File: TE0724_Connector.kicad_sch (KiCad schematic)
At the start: 2 parts, among them J1 SS5-80-3.50-L-D-K-TR, J3 Conn_02x05_Odd_Even

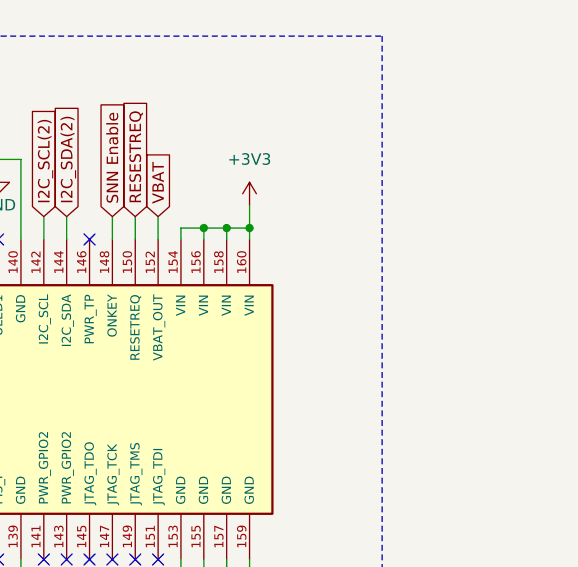
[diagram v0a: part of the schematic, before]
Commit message: Added some decoup caps and reviewed PCB layout
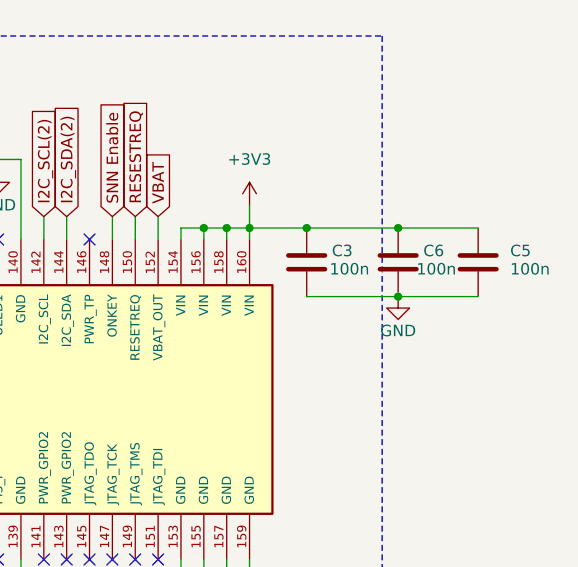
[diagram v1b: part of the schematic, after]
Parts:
- added C3, C5, C6: 100n, Capacitor_SMD:C_0603_1608Metric, symbol Device:C
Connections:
- net +3V3: now also C3.1, C5.1, C6.1
- net GND: now also C3.2, C5.2, C6.2

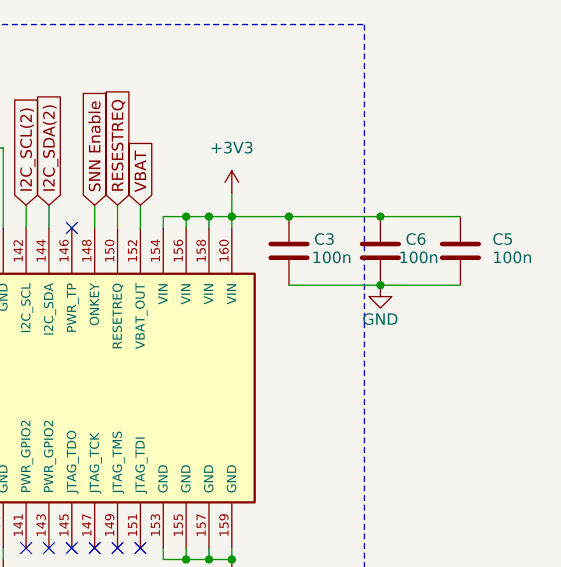
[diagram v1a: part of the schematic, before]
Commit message: removed some decoup caps because I added to many haha
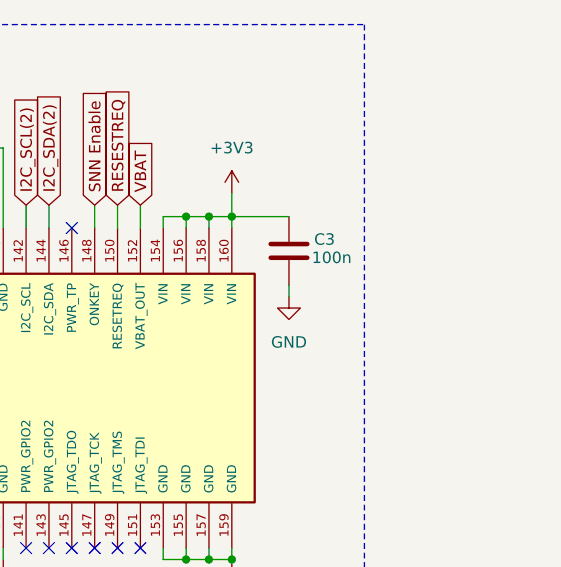
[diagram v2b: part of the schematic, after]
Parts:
- removed C5, C6: 100n, Capacitor_SMD:C_0603_1608Metric, symbol Device:C

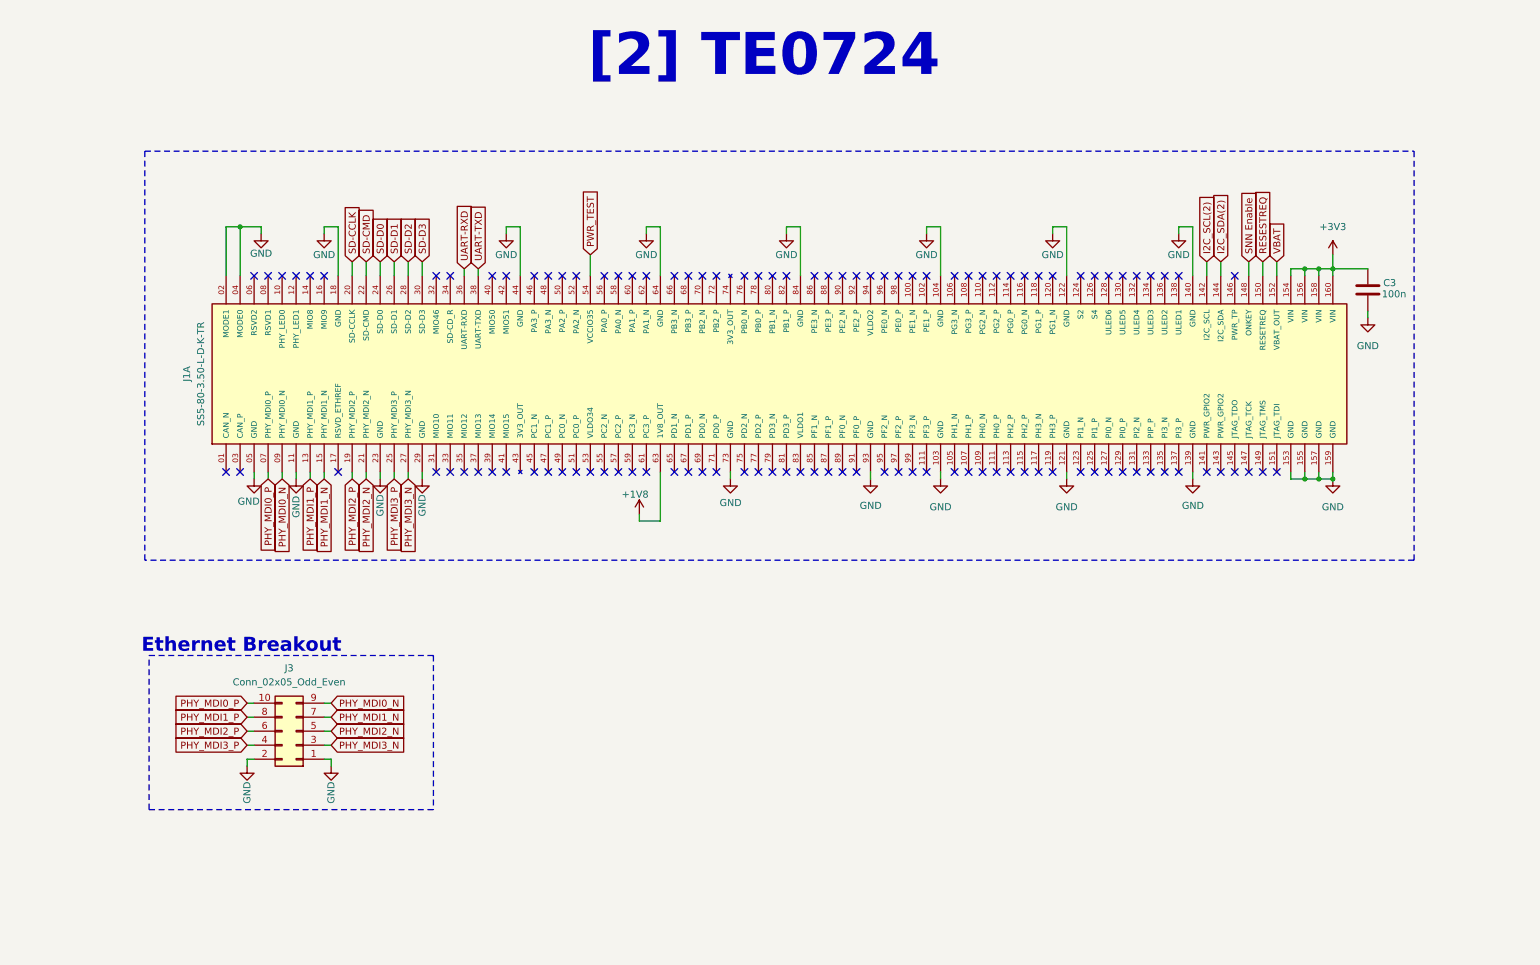
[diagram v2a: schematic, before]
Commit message: Added Level Shifter for SD card
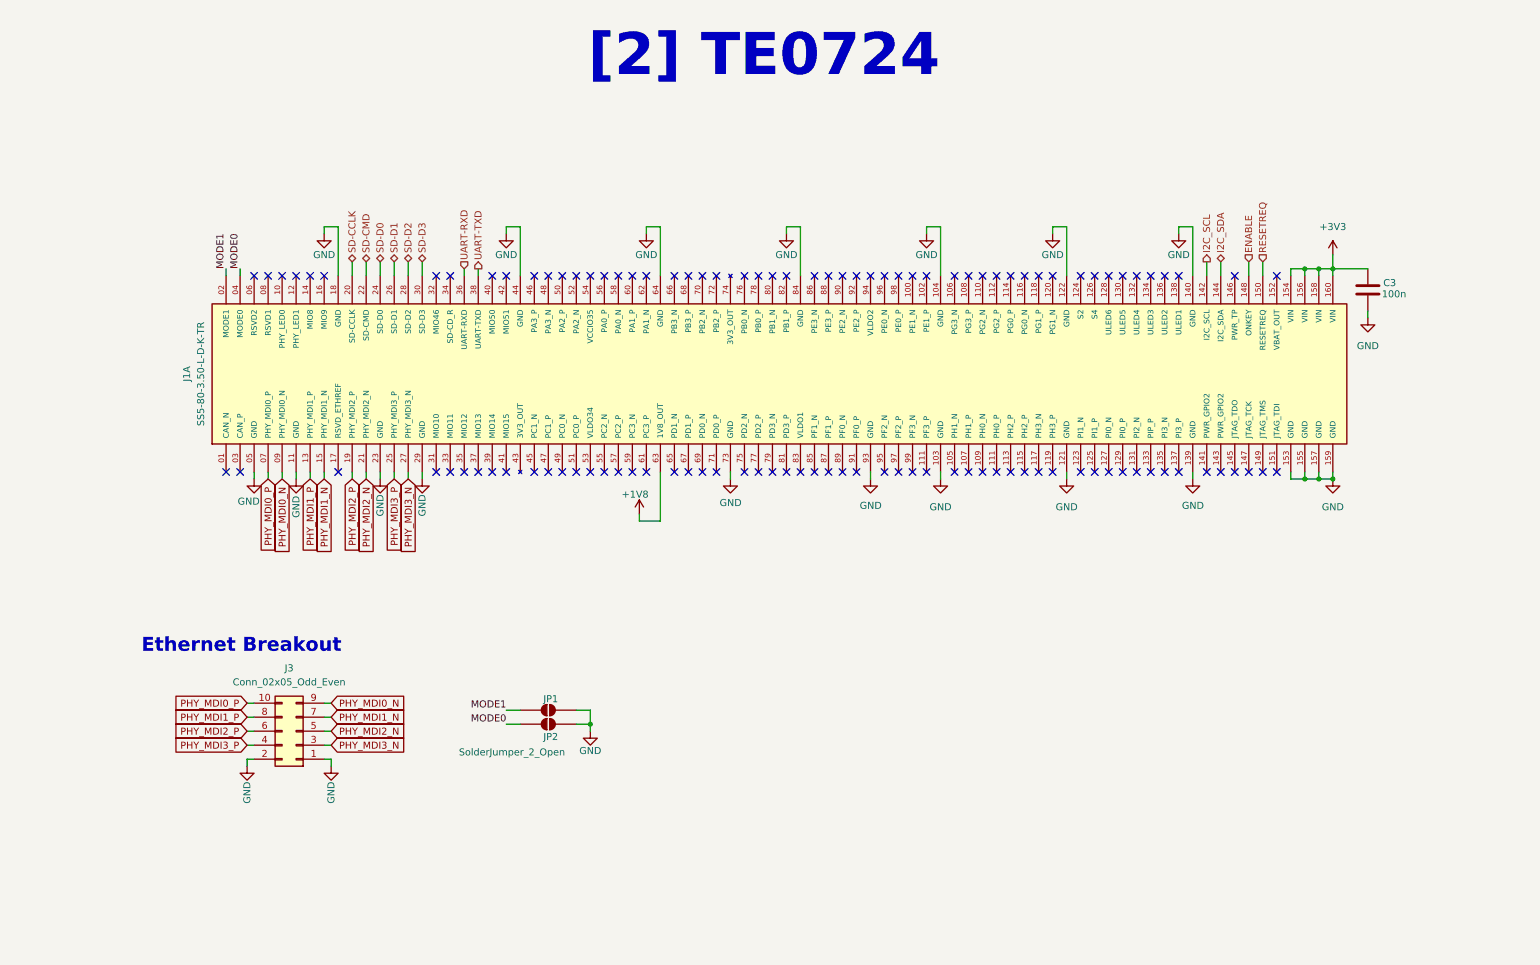
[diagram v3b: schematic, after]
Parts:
- added JP1, JP2: SolderJumper_2_Open, Jumper:SolderJumper-2_P1.3mm_Open_RoundedPad1.0x1.5mm, symbol Jumper:SolderJumper_2_Open
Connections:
- net GND: now also JP1.2 (B), JP2.2 (B); no longer J1.02 (MODE1), J1.04 (MODE0)
- net I2C_SCL(2) renamed I2C_SCL
- net I2C_SDA(2) renamed I2C_SDA
- net PWR_TEST: no longer names the net of J1.54 (VCCIO35)
- net RESESTREQ renamed RESETREQ
- net SNN Enable renamed ENABLE
- net VBAT: no longer names the net of J1.152 (VBAT_OUT)
- new net MODE0: J1.04 (MODE0), JP2.1 (A)
- new net MODE1: J1.02 (MODE1), JP1.1 (A)
- no-connect marks 109 -> 111

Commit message: Added pcb files for ethernet breakout board
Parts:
- J1: MPN (none) -> C5292077
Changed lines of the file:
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@@
+			)
+		)
+		(property "External Part Number" ""
+			(at 97.79 85.09 0)
+			(hide yes)
+			(show_name no)
+			(do_not_autoplace no)
+			(effects
+				(font
+					(size 1.27 1.27)
+				)
+			)
+		)
+		(property "MPN" "C5292077"
+			(at 97.79 85.09 0)
+			(hide yes)
+			(show_name no)
+			(do_not_autoplace no)
+			(effects
+				(font
+					(size 1.27 1.27)
+				)
 			)
 		)
@@
 			)
 		)
+		(property "External Part Number" ""
+			(at 107.95 148.59 0)
+			(hide yes)
+			(show_name no)
+			(do_not_autoplace no)
+			(effects
+				(font
+					(size 1.27 1.27)
+				)
+			)
+		)
+		(property "MPN" ""
+			(at 107.95 148.59 0)
+			(hide yes)
+			(show_name no)
+			(do_not_autoplace no)
+			(effects
+				(font
+					(size 1.27 1.27)
+				)
+			)
+		)
 		(pin "1"
 		)
@@
 			)
 		)
+		(property "External Part Number" ""
+			(at 107.95 146.05 0)
+			(hide yes)
+			(show_name no)
+			(do_not_autoplace no)
+			(effects
+				(font
+					(size 1.27 1.27)
+				)
+			)
+		)
+		(property "MPN" ""
+			(at 107.95 146.05 0)
+			(hide yes)
+			(show_name no)
+			(do_not_autoplace no)
+			(effects
+				(font
+					(size 1.27 1.27)
+				)
+			)
+		)
 		(pin "1"
 		)
@@
 		)
 		(property "MANUFACTURER_PART_NUMBER" "GCM155R71H104KE02D"
+			(at 256.54 69.85 0)
+			(hide yes)
+			(show_name no)
+			(do_not_autoplace no)
+			(effects
+				(font
+					(size 1.27 1.27)
+				)
+			)
+		)
+		(property "External Part Number" ""
+			(at 256.54 69.85 0)
+			(hide yes)
+			(show_name no)
+			(do_not_autoplace no)
+			(effects
+				(font
+					(size 1.27 1.27)
+				)
+			)
+		)
+		(property "MPN" ""
 			(at 256.54 69.85 0)
 			(hide yes)
@@
 			(at 62.23 149.86 0)
 			(hide yes)
+			(show_name no)
+			(do_not_autoplace no)
+			(effects
+				(font
+					(size 1.27 1.27)
+				)
+			)
+		)
+		(property "External Part Number" ""
+			(at 62.23 149.86 0)
+			(hide yes)
+			(show_name no)
+			(do_not_autoplace no)
+			(effects
+				(font
+					(size 1.27 1.27)
+				)
+			)
+		)
+		(property "MPN" ""
+			(at 62.23 149.86 0)
+			(hide yes)

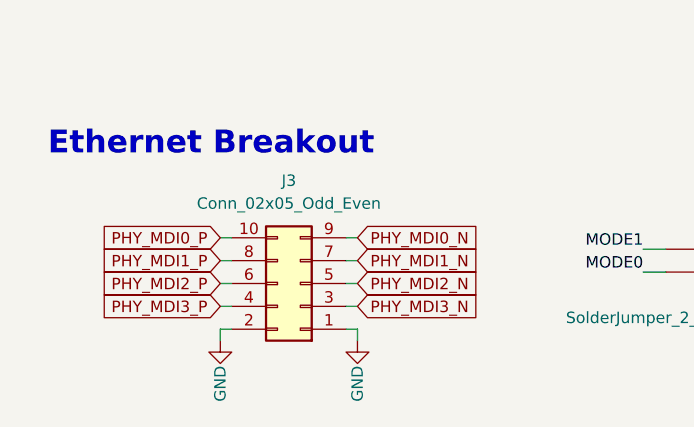
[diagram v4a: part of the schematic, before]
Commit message: Updated BOM and added fiducials
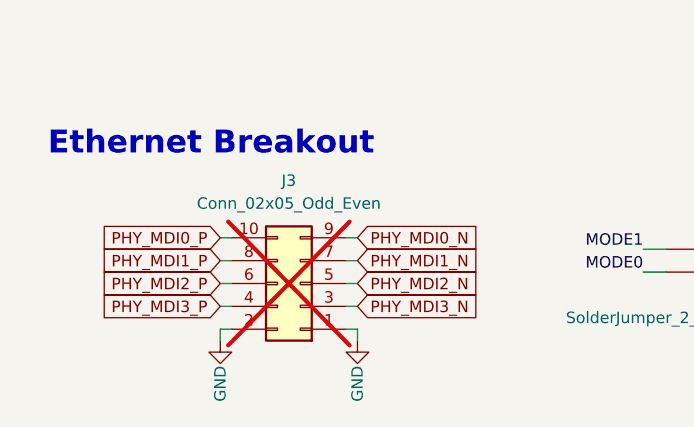
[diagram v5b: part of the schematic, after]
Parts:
- C3: External Part Number (none) -> GCM188R71H104KA57J; MANUFACTURER_PART_NUMBER GCM155R71H104KE02D -> (none); MPN (none) -> C3011652
- J1: External Part Number (none) -> SS5-80-3.50-L-D-K-TR; MANUFACTURER_PART_NUMBER SS5-80-3.50-L-D-K-TR -> (none)
- J3: now not fitted
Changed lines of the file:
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@@
 			)
 		)
-		(property "MANUFACTURER_PART_NUMBER" "SS5-80-3.50-L-D-K-TR "
-			(at 97.79 80.01 0)
-			(hide yes)
-			(show_name no)
-			(do_not_autoplace no)
-			(effects
-				(font
-					(size 1.27 1.27)
-				)
-			)
-		)
-		(property "External Part Number" ""
+		(property "External Part Number" "SS5-80-3.50-L-D-K-TR "
 			(at 97.79 85.09 0)
 			(hide yes)
@@
 			)
 		)
-		(property "MANUFACTURER_PART_NUMBER" "GCM155R71H104KE02D"
+		(property "External Part Number" "GCM188R71H104KA57J"
 			(at 256.54 69.85 0)
 			(hide yes)
@@
 			)
 		)
-		(property "External Part Number" ""
-			(at 256.54 69.85 0)
-			(hide yes)
-			(show_name no)
-			(do_not_autoplace no)
-			(effects
-				(font
-					(size 1.27 1.27)
-				)
-			)
-		)
-		(property "MPN" ""
+		(property "MPN" "C3011652"
 			(at 256.54 69.85 0)
 			(hide yes)
@@
 		(on_board yes)
 		(in_pos_files yes)
-		(dnp no)
+		(dnp yes)
 		(fields_autoplaced yes)
 		(property "Reference" "J3"

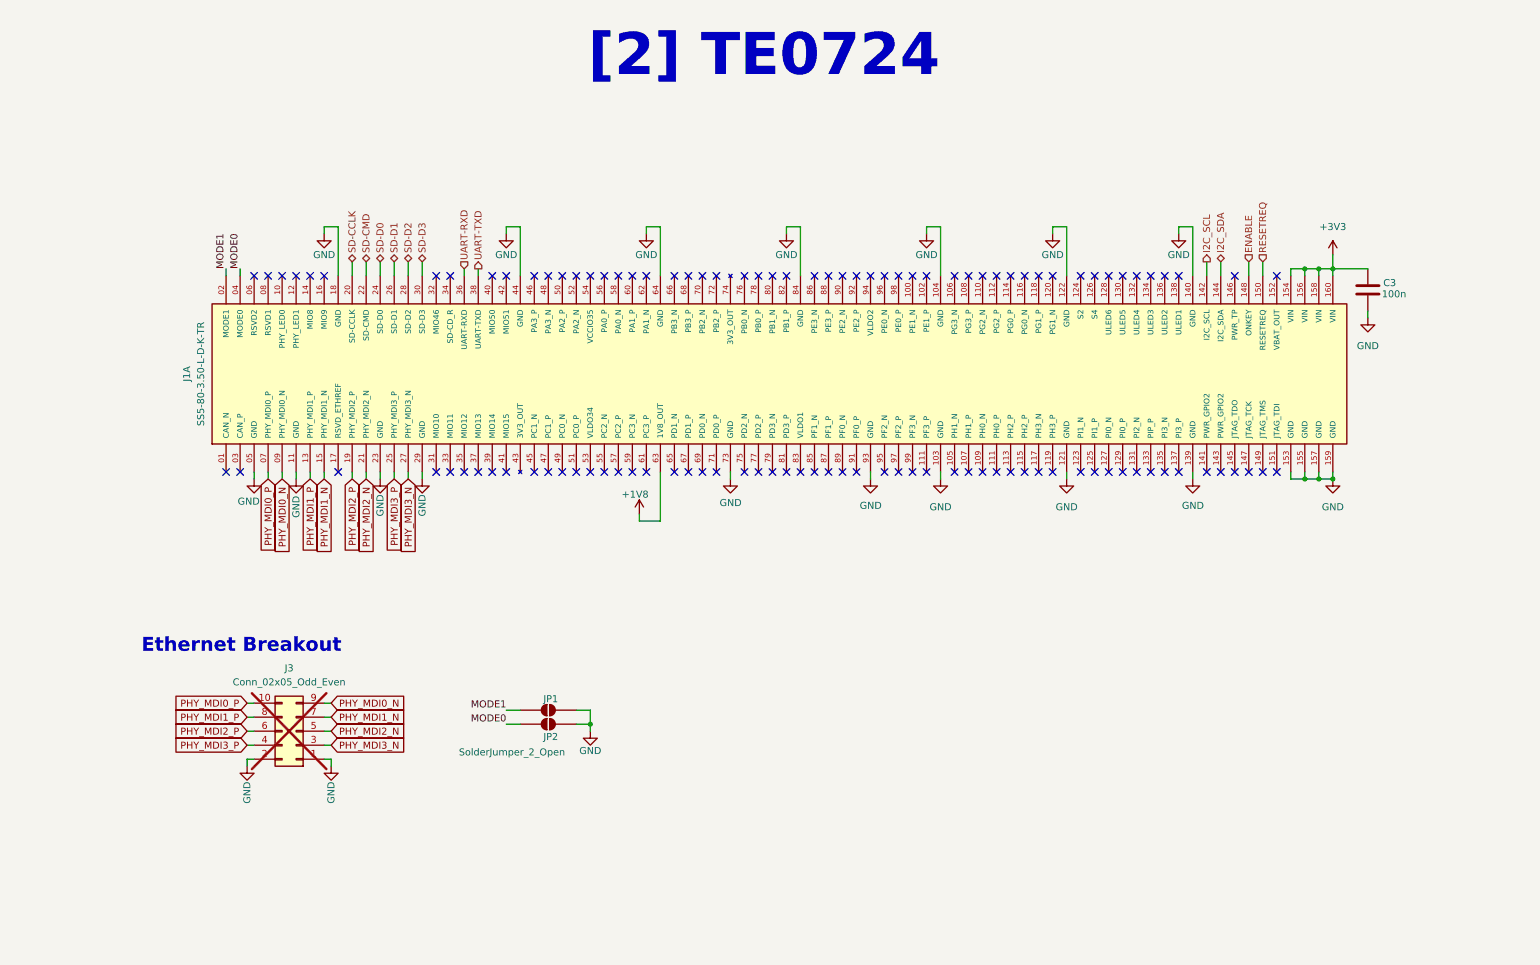
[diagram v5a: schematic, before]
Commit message: Changed connector orientation and power changes
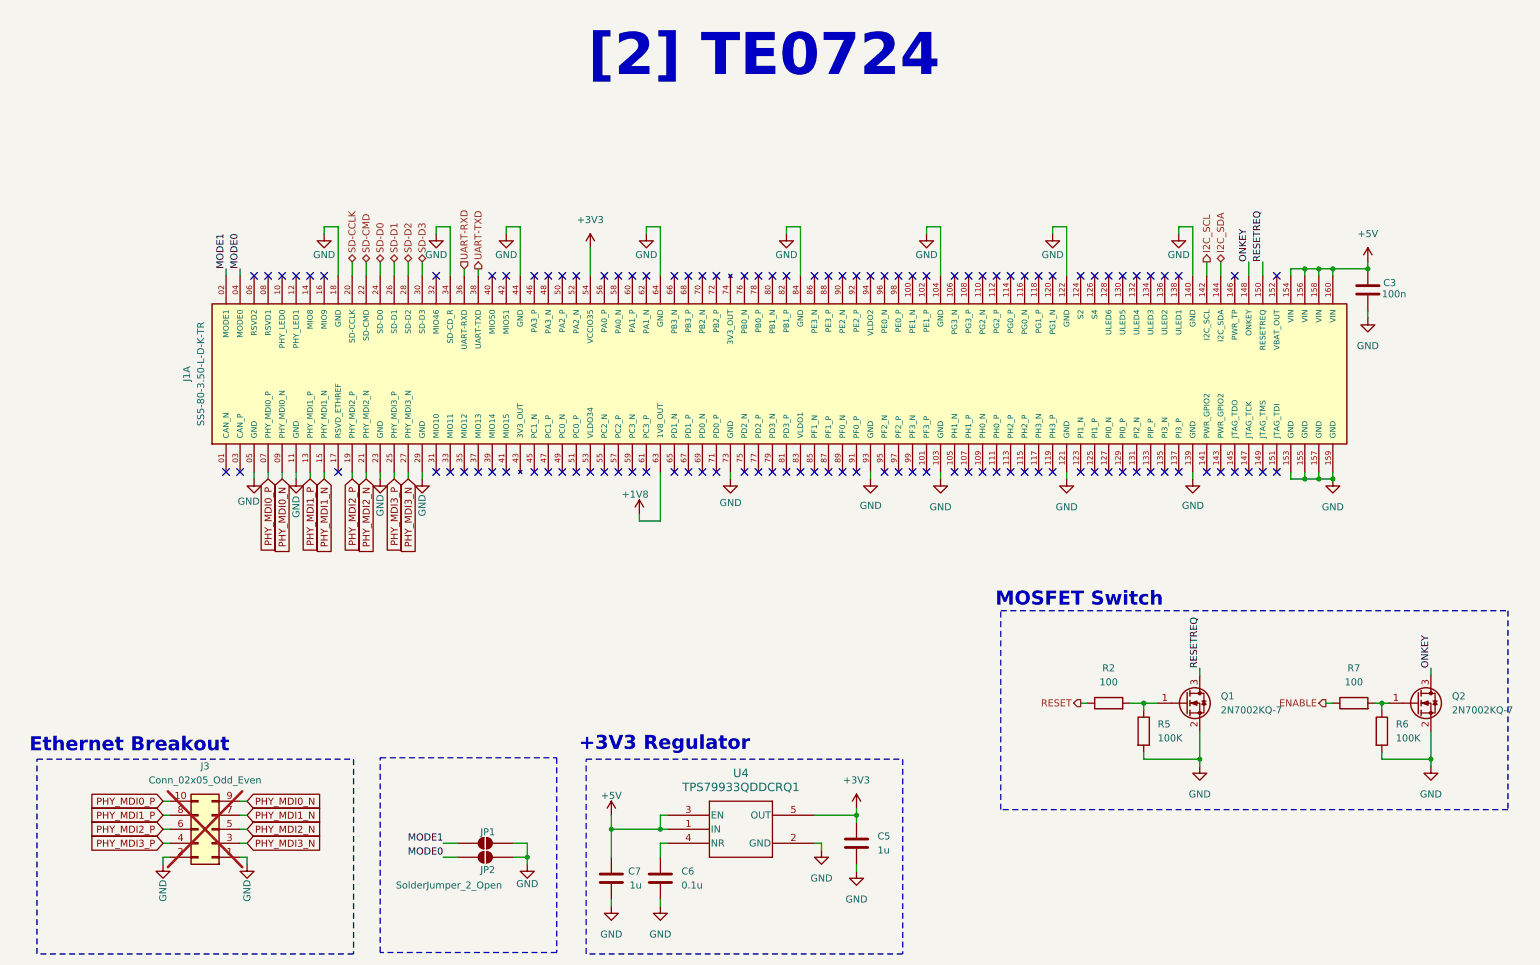
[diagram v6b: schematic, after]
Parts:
- added C5, C7: 1u, Capacitor_SMD:C_1206_3216Metric, symbol Device:C
- added C6: 0.1u, Capacitor_SMD:C_0603_1608Metric, symbol Device:C
- added Q1, Q2: 2N7002KQ-7, Package_TO_SOT_SMD:SOT-23, symbol Transistor_FET:2N7002K
- added R2, R7: 100, Resistor_SMD:R_0402_1005Metric, symbol Device:R
- added R5, R6: 100K, Resistor_SMD:R_0402_1005Metric, symbol Device:R
- added U4: TPS79933QDDCRQ1, adapter:DDC5, symbol adapter:TPS79933QDDCRQ1
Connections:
- net +3V3: now also J1.54 (VCCIO35), C5.1, U4.5 (OUT); no longer C3.1, J1.154 (VIN), J1.156 (VIN), J1.158 (VIN), J1.160 (VIN)
- net ENABLE: now also R7.1; no longer J1.148 (ONKEY)
- net GND: now also J1.34 (SD-CD_R), C5.2, C6.2, C7.2, Q1.2 (S), Q2.2 (S), R5.2, R6.2, U4.2 (GND)
- net RESETREQ: now also Q1.3 (D)
- new net: C6.1, U4.4 (NR)
- new net: Q2.1 (G), R6.1, R7.2
- new net: Q1.1 (G), R2.2, R5.1
- new net +5V: C3.1, C7.1, J1.154 (VIN), J1.156 (VIN), J1.158 (VIN), J1.160 (VIN), U4.1 (IN), U4.3 (EN)
- new net ONKEY: J1.148 (ONKEY), Q2.3 (D)
- new net RESET: R2.1
- no-connect marks 111 -> 109
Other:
- note added: "+3V3 Regulator"
- note added: "MOSFET Switch"
- moved on the sheet: J3, JP1, JP2

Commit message: Made very tiny tweaks again
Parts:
- J3: now left out of the parts list
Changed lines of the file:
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@@
 		(body_style 1)
 		(exclude_from_sim no)
-		(in_bom yes)
-		(on_board yes)
-		(in_pos_files yes)
+		(in_bom no)
+		(on_board no)
+		(in_pos_files no)
 		(dnp yes)
 		(fields_autoplaced yes)
